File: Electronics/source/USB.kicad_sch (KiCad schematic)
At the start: 9 parts, among them J5 Conn_01x05, P1 USB_C_Plug_USB2.0

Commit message: added mechanical ignore
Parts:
- P1: footprint Connector_USB:USB_C_Receptacle_GCT_USB4085 -> Connector_USB:USB_C_Receptacle_HRO_TYPE-C-31-M-12
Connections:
- net +5V: now also D3.1 (A1); no longer D3.2 (A2)
- net GND: now also D1.2 (A2), D2.2 (A2), D3.2 (A2); no longer D1.1 (A1), D2.1 (A1), D3.1 (A1)
- net at J5.4 (Pin_4), P1.A6 (D+): now also D2.1 (A1); no longer D2.2 (A2)
- net at J5.3 (Pin_3), P1.A7 (D-): now also D1.1 (A1); no longer D1.2 (A2)
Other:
- moved on the sheet: D1, D2, D3
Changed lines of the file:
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@@
     (pin "2")
   )
-  (symbol (lib_id "Diode:ESD9B3.3ST5G") (at 140.97 77.47 90) (unit 1)
+  (symbol (lib_id "Diode:ESD9B3.3ST5G") (at 140.97 77.47 270) (unit 1)
     (in_bom yes) (on_board yes) (fields_autoplaced)
     (property "Reference" "D2" (id 0) (at 143.51 76.1999 90)
-      (effects (font (size 1.27 1.27)) (justify right))
+      (effects (font (size 1.27 1.27)) (justify left))
     )
     (property "Value" "ESD9B3.3ST5G" (id 1) (at 143.51 78.7399 90)
-      (effects (font (size 1.27 1.27)) (justify right))
+      (effects (font (size 1.27 1.27)) (justify left))
     )
     (property "Footprint" "Diode_SMD:D_SOD-923" (id 2) (at 140.97 77.47 0)
@@
     (property "Reference" "P1" (id 0) (at 113.03 48.26 0))
     (property "Value" "USB_C_Plug_USB2.0" (id 1) (at 113.03 50.8 0))
-    (property "Footprint" "Connector_USB:USB_C_Receptacle_GCT_USB4085" (id 2) (at 116.84 71.12 0)
+    (property "Footprint" "Connector_USB:USB_C_Receptacle_HRO_TYPE-C-31-M-12" (id 2) (at 116.84 71.12 0)
       (effects (font (size 1.27 1.27)) hide)
     )
@@
     (pin "1")
   )
-  (symbol (lib_id "Diode:ESD9B3.3ST5G") (at 134.62 72.39 90) (unit 1)
+  (symbol (lib_id "Diode:ESD9B3.3ST5G") (at 134.62 72.39 270) (unit 1)
     (in_bom yes) (on_board yes) (fields_autoplaced)
     (property "Reference" "D1" (id 0) (at 137.16 71.1199 90)
-      (effects (font (size 1.27 1.27)) (justify right))
+      (effects (font (size 1.27 1.27)) (justify left))
     )
     (property "Value" "ESD9B3.3ST5G" (id 1) (at 137.16 73.6599 90)
-      (effects (font (size 1.27 1.27)) (justify right))
+      (effects (font (size 1.27 1.27)) (justify left))
     )
     (property "Footprint" "Diode_SMD:D_SOD-923" (id 2) (at 134.62 72.39 0)
@@
     (pin "1")
   )
-  (symbol (lib_id "Diode:ESD9B5.0ST5G") (at 153.67 52.07 90) (unit 1)
+  (symbol (lib_id "Diode:ESD9B5.0ST5G") (at 153.67 52.07 270) (unit 1)
     (in_bom yes) (on_board yes) (fields_autoplaced)
     (property "Reference" "D3" (id 0) (at 156.21 50.7999 90)
-      (effects (font (size 1.27 1.27)) (justify right))
+      (effects (font (size 1.27 1.27)) (justify left))
     )
     (property "Value" "ESD9B5.0ST5G" (id 1) (at 156.21 53.3399 90)
-      (effects (font (size 1.27 1.27)) (justify right))
+      (effects (font (size 1.27 1.27)) (justify left))
     )
     (property "Footprint" "Diode_SMD:D_SOD-923" (id 2) (at 153.67 52.07 0)

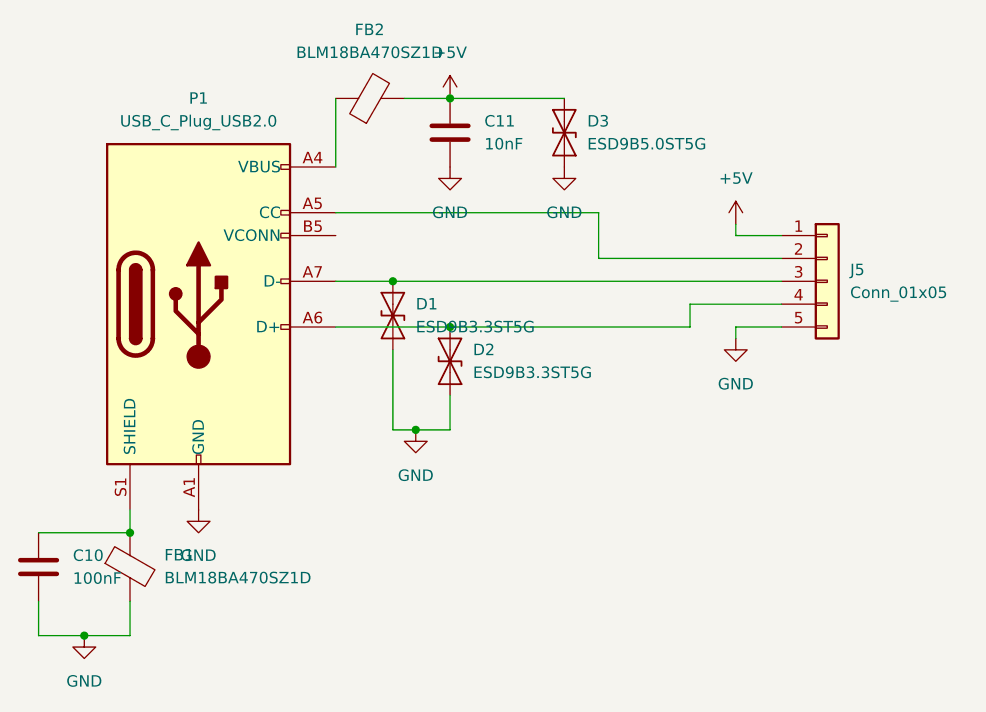
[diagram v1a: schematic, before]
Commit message: small bug fixes and clock stability
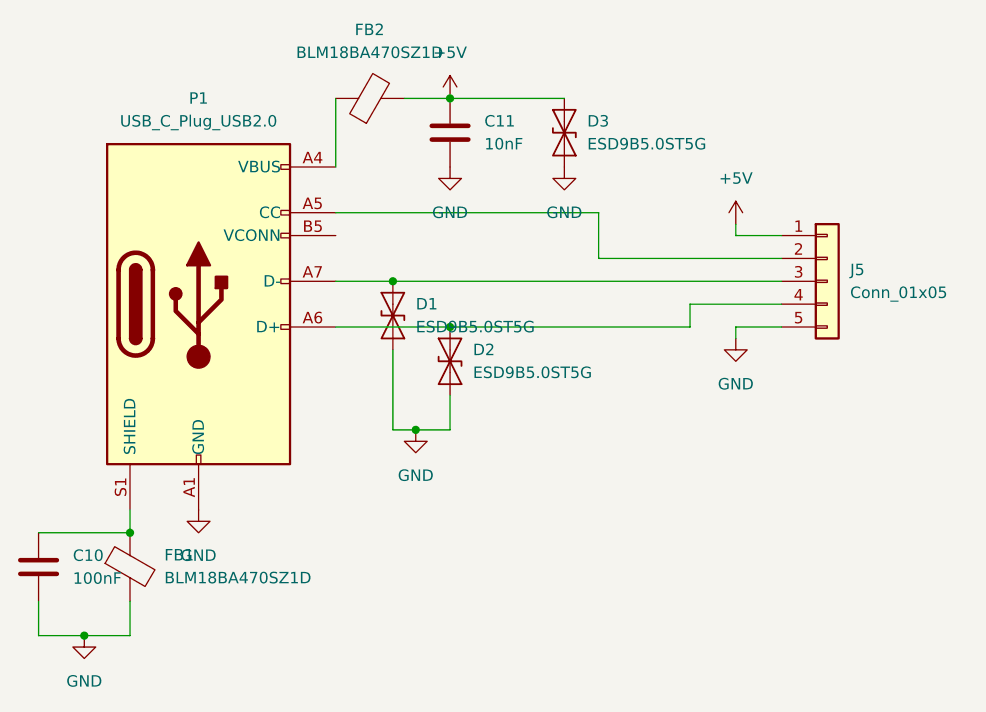
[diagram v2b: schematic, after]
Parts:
- removed D1, D2: ESD9B3.3ST5G, Diode_SMD:D_SOD-923, symbol Diode:ESD9B3.3ST5G
- added D1, D2: ESD9B5.0ST5G, Diode_SMD:D_SOD-923, symbol Diode:ESD9B5.0ST5G
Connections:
- net GND: now also D1.1 (A1), D2.2 (A2)
- net at J5.4 (Pin_4), P1.A6 (D+): now also D2.1 (A1)
- net at J5.3 (Pin_3), P1.A7 (D-): now also D1.2 (A2)
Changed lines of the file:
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@@
     (rev "v0.1")
   )
+  (junction (at 105.41 96.52) (diameter 0) (color 0 0 0 0)
+  )
+  (junction (at 134.62 68.58) (diameter 0) (color 0 0 0 0)
+  )
+  (junction (at 137.16 85.09) (diameter 0) (color 0 0 0 0)
+  )
   (junction (at 140.97 73.66) (diameter 0) (color 0 0 0 0)
   )
-  (junction (at 105.41 96.52) (diameter 0) (color 0 0 0 0)
-  )
-  (junction (at 137.16 85.09) (diameter 0) (color 0 0 0 0)
-  )
-  (junction (at 134.62 68.58) (diameter 0) (color 0 0 0 0)
-  )
   (junction (at 100.33 107.95) (diameter 0) (color 0 0 0 0)
   )
@@
     (stroke (width 0) (type default) (color 0 0 0 0))
   )
+  (wire (pts (xy 95.25 104.14) (xy 95.25 107.95))
+    (stroke (width 0) (type default) (color 0 0 0 0))
+  )
+  (wire (pts (xy 100.33 107.95) (xy 105.41 107.95))
+    (stroke (width 0) (type default) (color 0 0 0 0))
+  )
+  (wire (pts (xy 172.72 62.23) (xy 172.72 63.5))
+    (stroke (width 0) (type default) (color 0 0 0 0))
+  )
+  (wire (pts (xy 135.89 48.26) (xy 140.97 48.26))
+    (stroke (width 0) (type default) (color 0 0 0 0))
+  )
+  (wire (pts (xy 172.72 73.66) (xy 172.72 74.93))
+    (stroke (width 0) (type default) (color 0 0 0 0))
+  )
+  (wire (pts (xy 140.97 85.09) (xy 140.97 81.28))
+    (stroke (width 0) (type default) (color 0 0 0 0))
+  )
+  (wire (pts (xy 134.62 68.58) (xy 177.8 68.58))
+    (stroke (width 0) (type default) (color 0 0 0 0))
+  )
   (wire (pts (xy 140.97 73.66) (xy 167.64 73.66))
-    (stroke (width 0) (type default) (color 0 0 0 0))
-  )
-  (wire (pts (xy 95.25 104.14) (xy 95.25 107.95))
-    (stroke (width 0) (type default) (color 0 0 0 0))
-  )
-  (wire (pts (xy 100.33 107.95) (xy 105.41 107.95))
-    (stroke (width 0) (type default) (color 0 0 0 0))
-  )
-  (wire (pts (xy 172.72 62.23) (xy 172.72 63.5))
-    (stroke (width 0) (type default) (color 0 0 0 0))
-  )
-  (wire (pts (xy 134.62 68.58) (xy 177.8 68.58))
-    (stroke (width 0) (type default) (color 0 0 0 0))
-  )
-  (wire (pts (xy 135.89 48.26) (xy 140.97 48.26))
-    (stroke (width 0) (type default) (color 0 0 0 0))
-  )
-  (wire (pts (xy 172.72 73.66) (xy 172.72 74.93))
-    (stroke (width 0) (type default) (color 0 0 0 0))
-  )
-  (wire (pts (xy 140.97 85.09) (xy 140.97 81.28))
     (stroke (width 0) (type default) (color 0 0 0 0))
   )
@@
     (pin "2")
   )
-  (symbol (lib_id "Diode:ESD9B3.3ST5G") (at 140.97 77.47 270) (unit 1)
-    (in_bom yes) (on_board yes) (fields_autoplaced)
-    (property "Reference" "D2" (id 0) (at 143.51 76.1999 90)
-      (effects (font (size 1.27 1.27)) (justify left))
-    )
-    (property "Value" "ESD9B3.3ST5G" (id 1) (at 143.51 78.7399 90)
-      (effects (font (size 1.27 1.27)) (justify left))
-    )
-    (property "Footprint" "Diode_SMD:D_SOD-923" (id 2) (at 140.97 77.47 0)
-      (effects (font (size 1.27 1.27)) hide)
-    )
-    (property "Datasheet" "https://www.onsemi.com/pub/Collateral/ESD9B-D.PDF" (id 3) (at 140.97 77.47 0)
+  (symbol (lib_id "Diode:ESD9B5.0ST5G") (at 134.62 72.39 90) (unit 1)
+    (in_bom yes) (on_board yes) (fields_autoplaced)
+    (property "Reference" "D1" (id 0) (at 137.16 71.1199 90)
+      (effects (font (size 1.27 1.27)) (justify right))
+    )
+    (property "Value" "ESD9B5.0ST5G" (id 1) (at 137.16 73.6599 90)
+      (effects (font (size 1.27 1.27)) (justify right))
+    )
+    (property "Footprint" "Diode_SMD:D_SOD-923" (id 2) (at 134.62 72.39 0)
+      (effects (font (size 1.27 1.27)) hide)
+    )
+    (property "Datasheet" "https://www.onsemi.com/pub/Collateral/ESD9B-D.PDF" (id 3) (at 134.62 72.39 0)
       (effects (font (size 1.27 1.27)) hide)
     )
@@
     (pin "1")
   )
-  (symbol (lib_id "Diode:ESD9B3.3ST5G") (at 134.62 72.39 270) (unit 1)
-    (in_bom yes) (on_board yes) (fields_autoplaced)
-    (property "Reference" "D1" (id 0) (at 137.16 71.1199 90)
-      (effects (font (size 1.27 1.27)) (justify left))
-    )
-    (property "Value" "ESD9B3.3ST5G" (id 1) (at 137.16 73.6599 90)
-      (effects (font (size 1.27 1.27)) (justify left))
-    )
-    (property "Footprint" "Diode_SMD:D_SOD-923" (id 2) (at 134.62 72.39 0)
-      (effects (font (size 1.27 1.27)) hide)
-    )
-    (property "Datasheet" "https://www.onsemi.com/pub/Collateral/ESD9B-D.PDF" (id 3) (at 134.62 72.39 0)
-      (effects (font (size 1.27 1.27)) hide)
-    )
-    (pin "1")
-    (pin "2")
-  )
   (symbol (lib_id "Device:FerriteBead") (at 132.08 48.26 90) (unit 1)
     (in_bom yes) (on_board yes) (fields_autoplaced)
@@
     (pin "1")
   )
+  (symbol (lib_id "Diode:ESD9B5.0ST5G") (at 140.97 77.47 270) (unit 1)
+    (in_bom yes) (on_board yes) (fields_autoplaced)
+    (property "Reference" "D2" (id 0) (at 143.51 76.1999 90)
+      (effects (font (size 1.27 1.27)) (justify left))
+    )
+    (property "Value" "ESD9B5.0ST5G" (id 1) (at 143.51 78.7399 90)
+      (effects (font (size 1.27 1.27)) (justify left))
+    )
+    (property "Footprint" "Diode_SMD:D_SOD-923" (id 2) (at 140.97 77.47 0)
+      (effects (font (size 1.27 1.27)) hide)
+    )
+    (property "Datasheet" "https://www.onsemi.com/pub/Collateral/ESD9B-D.PDF" (id 3) (at 140.97 77.47 0)
+      (effects (font (size 1.27 1.27)) hide)
+    )
+    (pin "1")
+    (pin "2")
+  )
 )

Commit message: corrected incomplete USB for flipable cable, and replaced termination resistors w jumpers
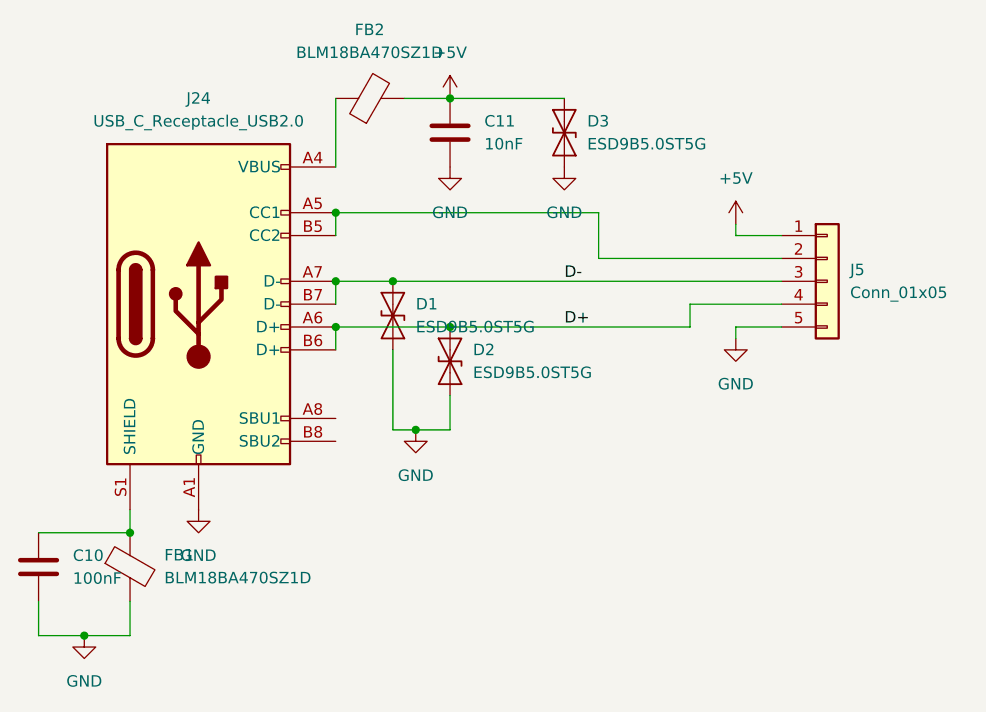
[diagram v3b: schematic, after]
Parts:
- removed P1: USB_C_Plug_USB2.0, Connector_USB:USB_C_Receptacle_HRO_TYPE-C-31-M-12, symbol Connector:USB_C_Plug_USB2.0
- added J24: USB_C_Receptacle_USB2.0, Connector_USB:USB_C_Receptacle_HRO_TYPE-C-31-M-12, symbol Connector:USB_C_Receptacle_USB2.0
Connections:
- net GND: now also J24.A1 (GND), J24.A12 (GND), J24.B1 (GND), J24.B12 (GND)
- net at C10.1, FB1.1: now also J24.S1 (SHIELD)
- net D-: now reaches D1.2 (A2), J5.3 (Pin_3)
- net D-: now also J24.A7 (D-), J24.B7 (D-)
- net at FB2.1: now also J24.A4 (VBUS), J24.A9 (VBUS), J24.B4 (VBUS), J24.B9 (VBUS)
- net at J5.2 (Pin_2): now also J24.A5 (CC1), J24.B5 (CC2)
- net D+: now reaches D2.1 (A1), J5.4 (Pin_4)
- net D+: now also J24.A6 (D+), J24.B6 (D+)
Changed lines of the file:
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@@
     (rev "v0.1")
   )
+  (junction (at 128.27 73.66) (diameter 0) (color 0 0 0 0)
+  )
   (junction (at 105.41 96.52) (diameter 0) (color 0 0 0 0)
   )
@@
   (junction (at 140.97 73.66) (diameter 0) (color 0 0 0 0)
   )
+  (junction (at 128.27 68.58) (diameter 0) (color 0 0 0 0)
+  )
+  (junction (at 128.27 60.96) (diameter 0) (color 0 0 0 0)
+  )
   (junction (at 100.33 107.95) (diameter 0) (color 0 0 0 0)
   )
@@
     (stroke (width 0) (type default) (color 0 0 0 0))
   )
+  (wire (pts (xy 128.27 68.58) (xy 128.27 71.12))
+    (stroke (width 0) (type default) (color 0 0 0 0))
+  )
   (wire (pts (xy 128.27 60.96) (xy 157.48 60.96))
     (stroke (width 0) (type default) (color 0 0 0 0))
@@
     (stroke (width 0) (type default) (color 0 0 0 0))
   )
+  (wire (pts (xy 128.27 60.96) (xy 128.27 63.5))
+    (stroke (width 0) (type default) (color 0 0 0 0))
+  )
   (wire (pts (xy 135.89 48.26) (xy 140.97 48.26))
     (stroke (width 0) (type default) (color 0 0 0 0))
@@
     (stroke (width 0) (type default) (color 0 0 0 0))
   )
+  (wire (pts (xy 128.27 73.66) (xy 128.27 76.2))
+    (stroke (width 0) (type default) (color 0 0 0 0))
+  )
   (wire (pts (xy 134.62 85.09) (xy 137.16 85.09))
     (stroke (width 0) (type default) (color 0 0 0 0))
@@
   (wire (pts (xy 167.64 71.12) (xy 167.64 73.66))
     (stroke (width 0) (type default) (color 0 0 0 0))
+  )
+  (label "D-" (at 153.67 68.58 0)
+    (effects (font (size 1.27 1.27)) (justify left bottom))
+  )
+  (label "D+" (at 153.67 73.66 0)
+    (effects (font (size 1.27 1.27)) (justify left bottom))
   )
   (symbol (lib_id "power:GND") (at 113.03 93.98 0) (unit 1)
@@
     (pin "1")
   )
-  (symbol (lib_id "Device:C") (at 95.25 100.33 0) (unit 1)
-    (in_bom yes) (on_board yes) (fields_autoplaced)
-    (property "Reference" "C10" (id 0) (at 99.06 99.0599 0)
-      (effects (font (size 1.27 1.27)) (justify left))
-    )
-    (property "Value" "100nF" (id 1) (at 99.06 101.5999 0)
-      (effects (font (size 1.27 1.27)) (justify left))
-    )
-    (property "Footprint" "Capacitor_SMD:C_0805_2012Metric" (id 2) (at 96.2152 104.14 0)
-      (effects (font (size 1.27 1.27)) hide)
-    )
-    (property "Datasheet" "~" (id 3) (at 95.25 100.33 0)
-      (effects (font (size 1.27 1.27)) hide)
-    )
-    (pin "1")
-    (pin "2")
-  )
-  (symbol (lib_id "Diode:ESD9B5.0ST5G") (at 134.62 72.39 90) (unit 1)
-    (in_bom yes) (on_board yes) (fields_autoplaced)
-    (property "Reference" "D1" (id 0) (at 137.16 71.1199 90)
-      (effects (font (size 1.27 1.27)) (justify right))
-    )
-    (property "Value" "ESD9B5.0ST5G" (id 1) (at 137.16 73.6599 90)
-      (effects (font (size 1.27 1.27)) (justify right))
-    )
-    (property "Footprint" "Diode_SMD:D_SOD-923" (id 2) (at 134.62 72.39 0)
-      (effects (font (size 1.27 1.27)) hide)
-    )
-    (property "Datasheet" "https://www.onsemi.com/pub/Collateral/ESD9B-D.PDF" (id 3) (at 134.62 72.39 0)
-      (effects (font (size 1.27 1.27)) hide)
-    )
-    (pin "1")
-    (pin "2")
-  )
-  (symbol (lib_id "power:GND") (at 172.72 74.93 0) (unit 1)
-    (in_bom yes) (on_board yes) (fields_autoplaced)
-    (property "Reference" "#PWR0103" (id 0) (at 172.72 81.28 0)
-      (effects (font (size 1.27 1.27)) hide)
-    )
-    (property "Value" "GND" (id 1) (at 172.72 80.01 0))
-    (property "Footprint" "" (id 2) (at 172.72 74.93 0)
-      (effects (font (size 1.27 1.27)) hide)
-    )
-    (property "Datasheet" "" (id 3) (at 172.72 74.93 0)
-      (effects (font (size 1.27 1.27)) hide)
-    )
-    (pin "1")
-  )
-  (symbol (lib_id "Device:FerriteBead") (at 105.41 100.33 0) (unit 1)
-    (in_bom yes) (on_board yes) (fields_autoplaced)
-    (property "Reference" "FB1" (id 0) (at 109.22 99.0091 0)
-      (effects (font (size 1.27 1.27)) (justify left))
-    )
-    (property "Value" "BLM18BA470SZ1D" (id 1) (at 109.22 101.5491 0)
-      (effects (font (size 1.27 1.27)) (justify left))
-    )
-    (property "Footprint" "Capacitor_SMD:C_0603_1608Metric" (id 2) (at 103.632 100.33 90)
-      (effects (font (size 1.27 1.27)) hide)
-    )
-    (property "Datasheet" "~" (id 3) (at 105.41 100.33 0)
-      (effects (font (size 1.27 1.27)) hide)
-    )
-    (pin "1")
-    (pin "2")
-  )
-  (symbol (lib_id "power:GND") (at 137.16 85.09 0) (unit 1)
-    (in_bom yes) (on_board yes) (fields_autoplaced)
-    (property "Reference" "#PWR0142" (id 0) (at 137.16 91.44 0)
-      (effects (font (size 1.27 1.27)) hide)
-    )
-    (property "Value" "GND" (id 1) (at 137.16 90.17 0))
-    (property "Footprint" "" (id 2) (at 137.16 85.09 0)
-      (effects (font (size 1.27 1.27)) hide)
-    )
-    (property "Datasheet" "" (id 3) (at 137.16 85.09 0)
-      (effects (font (size 1.27 1.27)) hide)
-    )
-    (pin "1")
-  )
-  (symbol (lib_id "Connector:USB_C_Plug_USB2.0") (at 113.03 71.12 0) (unit 1)
-    (in_bom yes) (on_board yes) (fields_autoplaced)
-    (property "Reference" "P1" (id 0) (at 113.03 48.26 0))
-    (property "Value" "USB_C_Plug_USB2.0" (id 1) (at 113.03 50.8 0))
+  (symbol (lib_id "Connector:USB_C_Receptacle_USB2.0") (at 113.03 71.12 0) (unit 1)
+    (in_bom yes) (on_board yes) (fields_autoplaced)
+    (property "Reference" "J24" (id 0) (at 113.03 48.26 0))
+    (property "Value" "USB_C_Receptacle_USB2.0" (id 1) (at 113.03 50.8 0))
     (property "Footprint" "Connector_USB:USB_C_Receptacle_HRO_TYPE-C-31-M-12" (id 2) (at 116.84 71.12 0)
       (effects (font (size 1.27 1.27)) hide)
@@
     (pin "A6")
     (pin "A7")
+    (pin "A8")
     (pin "A9")
     (pin "B1")
@@
     (pin "B4")
     (pin "B5")
+    (pin "B6")
+    (pin "B7")
+    (pin "B8")
     (pin "B9")
     (pin "S1")
   )
+  (symbol (lib_id "Device:C") (at 95.25 100.33 0) (unit 1)
+    (in_bom yes) (on_board yes) (fields_autoplaced)
+    (property "Reference" "C10" (id 0) (at 99.06 99.0599 0)
+      (effects (font (size 1.27 1.27)) (justify left))
+    )
+    (property "Value" "100nF" (id 1) (at 99.06 101.5999 0)
+      (effects (font (size 1.27 1.27)) (justify left))
+    )
+    (property "Footprint" "Capacitor_SMD:C_0805_2012Metric" (id 2) (at 96.2152 104.14 0)
+      (effects (font (size 1.27 1.27)) hide)
+    )
+    (property "Datasheet" "~" (id 3) (at 95.25 100.33 0)
+      (effects (font (size 1.27 1.27)) hide)
+    )
+    (pin "1")
+    (pin "2")
+  )
+  (symbol (lib_id "Diode:ESD9B5.0ST5G") (at 134.62 72.39 90) (unit 1)
+    (in_bom yes) (on_board yes) (fields_autoplaced)
+    (property "Reference" "D1" (id 0) (at 137.16 71.1199 90)
+      (effects (font (size 1.27 1.27)) (justify right))
+    )
+    (property "Value" "ESD9B5.0ST5G" (id 1) (at 137.16 73.6599 90)
+      (effects (font (size 1.27 1.27)) (justify right))
+    )
+    (property "Footprint" "Diode_SMD:D_SOD-923" (id 2) (at 134.62 72.39 0)
+      (effects (font (size 1.27 1.27)) hide)
+    )
+    (property "Datasheet" "https://www.onsemi.com/pub/Collateral/ESD9B-D.PDF" (id 3) (at 134.62 72.39 0)
+      (effects (font (size 1.27 1.27)) hide)
+    )
+    (pin "1")
+    (pin "2")
+  )
+  (symbol (lib_id "power:GND") (at 172.72 74.93 0) (unit 1)
+    (in_bom yes) (on_board yes) (fields_autoplaced)
+    (property "Reference" "#PWR0103" (id 0) (at 172.72 81.28 0)
+      (effects (font (size 1.27 1.27)) hide)
+    )
+    (property "Value" "GND" (id 1) (at 172.72 80.01 0))
+    (property "Footprint" "" (id 2) (at 172.72 74.93 0)
+      (effects (font (size 1.27 1.27)) hide)
+    )
+    (property "Datasheet" "" (id 3) (at 172.72 74.93 0)
+      (effects (font (size 1.27 1.27)) hide)
+    )
+    (pin "1")
+  )
+  (symbol (lib_id "Device:FerriteBead") (at 105.41 100.33 0) (unit 1)
+    (in_bom yes) (on_board yes) (fields_autoplaced)
+    (property "Reference" "FB1" (id 0) (at 109.22 99.0091 0)
+      (effects (font (size 1.27 1.27)) (justify left))
+    )
+    (property "Value" "BLM18BA470SZ1D" (id 1) (at 109.22 101.5491 0)
+      (effects (font (size 1.27 1.27)) (justify left))
+    )
+    (property "Footprint" "Capacitor_SMD:C_0603_1608Metric" (id 2) (at 103.632 100.33 90)
+      (effects (font (size 1.27 1.27)) hide)
+    )
+    (property "Datasheet" "~" (id 3) (at 105.41 100.33 0)
+      (effects (font (size 1.27 1.27)) hide)
+    )
+    (pin "1")
+    (pin "2")
+  )
+  (symbol (lib_id "power:GND") (at 137.16 85.09 0) (unit 1)
+    (in_bom yes) (on_board yes) (fields_autoplaced)
+    (property "Reference" "#PWR0142" (id 0) (at 137.16 91.44 0)
+      (effects (font (size 1.27 1.27)) hide)
+    )
+    (property "Value" "GND" (id 1) (at 137.16 90.17 0))
+    (property "Footprint" "" (id 2) (at 137.16 85.09 0)
+      (effects (font (size 1.27 1.27)) hide)
+    )
+    (property "Datasheet" "" (id 3) (at 137.16 85.09 0)
+      (effects (font (size 1.27 1.27)) hide)
+    )
+    (pin "1")
+  )
   (symbol (lib_id "power:GND") (at 153.67 55.88 0) (unit 1)
